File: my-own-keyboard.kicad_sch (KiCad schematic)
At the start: 138 parts, among them J1 CX70M-24P1, SW1 Reset SW, SW10 Key_SW, SW11 Key_SW, SW12 Key_SW, SW13 Key_SW, SW14 Key_SW, SW15 Key_SW, SW16 Key_SW, SW17 Key_SW, SW18 Key_SW, SW19 Key_SW, SW2 Key_SW, SW20 Key_SW, SW21 Key_SW, SW22 Key_SW, SW23 Key_SW, SW24 Key_SW, SW25 Key_SW, SW26 Key_SW, SW27 Key_SW, SW28 Key_SW, SW29 Key_SW, SW3 Key_SW, SW30 Key_SW, SW31 Key_SW, SW32 Key_SW, SW33 Key_SW, SW34 Key_SW, SW35 Key_SW, SW36 Key_SW, SW37 Key_SW, SW38 Key_SW, SW39 Key_SW, SW4 Key_SW, SW40 Key_SW, SW41 Key_SW, SW42 Key_SW, SW43 Key_SW, SW44 Key_SW, SW45 Key_SW, SW46 Key_SW, SW47 Key_SW, SW48 Key_SW, SW49 Key_SW, SW5 Key_SW, SW50 Key_SW, SW51 Key_SW, SW52 Key_SW, SW53 Key_SW, SW54 Key_SW, SW55 Key_SW, SW56 Key_SW, SW57 Key_SW, SW58 Key_SW, SW59 Key_SW, SW6 Key_SW, SW60 Key_SW, SW61 Key_SW, SW62 Key_SW, SW7 Key_SW, SW8 Key_SW, SW9 Key_SW, U1 ATmega32U4-A, Y1 16MHz

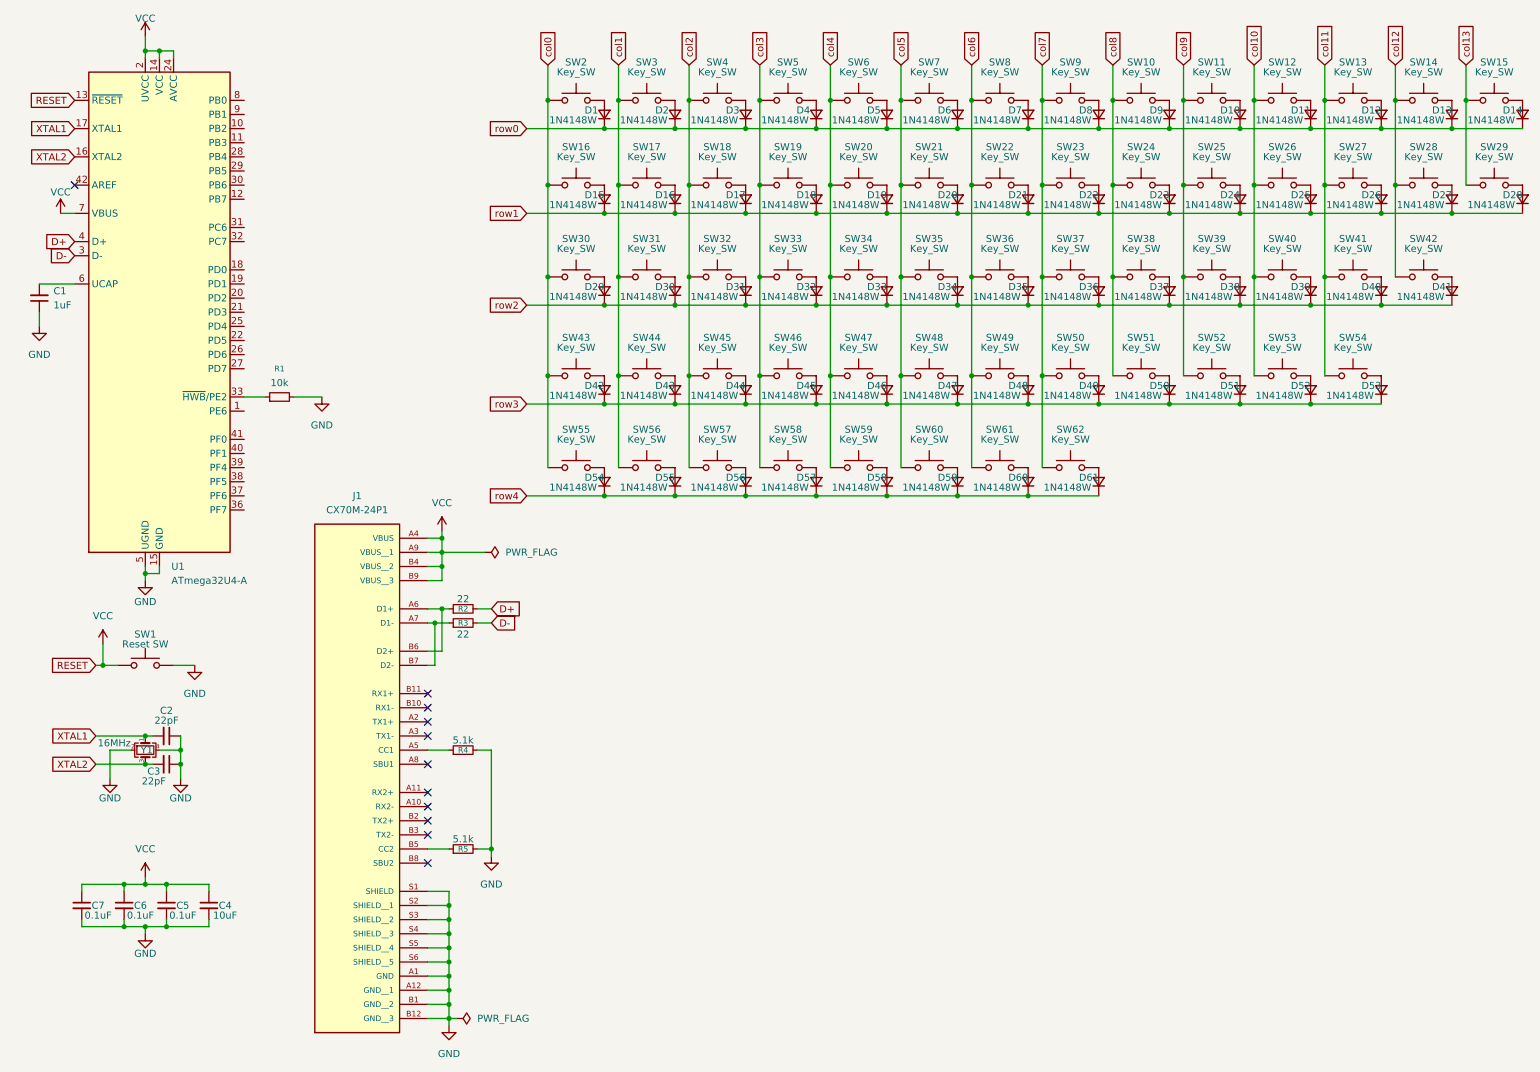
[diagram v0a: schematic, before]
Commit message: completed creating the first circuit
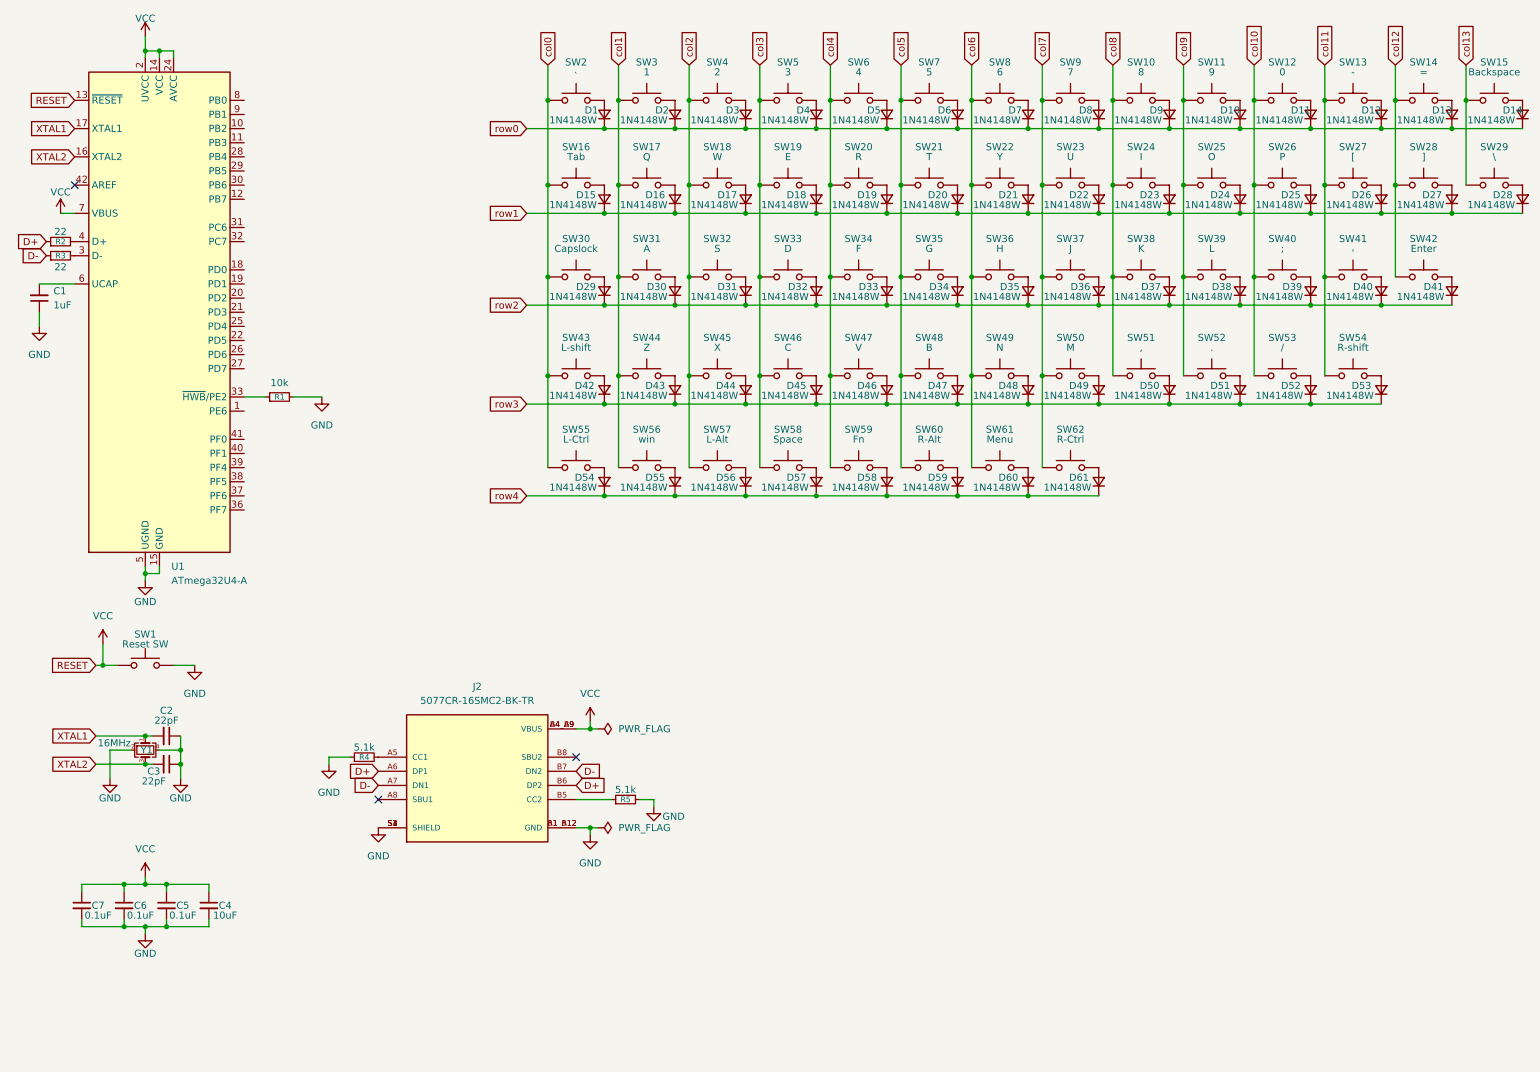
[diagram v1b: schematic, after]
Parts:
- removed J1: CX70M-24P1, CX70M-24P1:HRS_CX70M-24P1, symbol CX70M-24P1:CX70M-24P1
- added J2: 5077CR-16SMC2-BK-TR, 5077CR-16SMC2-BK-TR:NELTRON_5077CR-16SMC2-BK-TR, symbol 5077CR-16SMC2-BK-TR:5077CR-16SMC2-BK-TR
- C1, C2, C3, C4, C5, C6, C7: footprint (none) -> Capacitor_SMD:C_0603_1608Metric
- D1, D10, D11, D12, D13, D14, D15, D16, D17, D18, D19, D2, D20, D21, D22, D23, D24, D25, D26, D27, D28, D29, D3, D30, D31, D32, D33, D34, D35, D36, D37, D38, D39, D4, D40, D41, D42, D43, D44, D45, D46, D47, D48, D49, D5, D50, D51, D52, D53, D54, D55, D56, D57, D58, D59, D6, D60, D61, D7, D8, D9: footprint (none) -> kbd:D3_TH_SMD
- R1, R2, R3, R4, R5: footprint (none) -> Resistor_SMD:R_0603_1608Metric
- SW1: footprint (none) -> kbd:ResetSW
- SW10: value Key_SW -> 8; footprint (none) -> BrownSugar_KBD:CherryMX_Hotswap_via_1U
- SW11: value Key_SW -> 9; footprint (none) -> BrownSugar_KBD:CherryMX_Hotswap_via_1U
- SW12: value Key_SW -> 0; footprint (none) -> BrownSugar_KBD:CherryMX_Hotswap_via_1U
- SW13: value Key_SW -> -; footprint (none) -> BrownSugar_KBD:CherryMX_Hotswap_via_1U
- SW14: value Key_SW -> =; footprint (none) -> BrownSugar_KBD:CherryMX_Hotswap_via_1U
- SW15: value Key_SW -> Backspace; footprint (none) -> BrownSugar_KBD:CherryMX_Hotswap_via_2U
- SW16: value Key_SW -> Tab; footprint (none) -> BrownSugar_KBD:CherryMX_Hotswap_via_1.5U
- SW17: value Key_SW -> Q; footprint (none) -> BrownSugar_KBD:CherryMX_Hotswap_via_1U
- SW18: value Key_SW -> W; footprint (none) -> BrownSugar_KBD:CherryMX_Hotswap_via_1U
- SW19: value Key_SW -> E; footprint (none) -> BrownSugar_KBD:CherryMX_Hotswap_via_1U
- SW2: value Key_SW -> `; footprint (none) -> BrownSugar_KBD:CherryMX_Hotswap_via_1U
- SW20: value Key_SW -> R; footprint (none) -> BrownSugar_KBD:CherryMX_Hotswap_via_1U
- SW21: value Key_SW -> T; footprint (none) -> BrownSugar_KBD:CherryMX_Hotswap_via_1U
- SW22: value Key_SW -> Y; footprint (none) -> BrownSugar_KBD:CherryMX_Hotswap_via_1U
- SW23: value Key_SW -> U; footprint (none) -> BrownSugar_KBD:CherryMX_Hotswap_via_1U
- SW24: value Key_SW -> I; footprint (none) -> BrownSugar_KBD:CherryMX_Hotswap_via_1U
- SW25: value Key_SW -> O; footprint (none) -> BrownSugar_KBD:CherryMX_Hotswap_via_1U
- SW26: value Key_SW -> P; footprint (none) -> BrownSugar_KBD:CherryMX_Hotswap_via_1U
- SW27: value Key_SW -> [; footprint (none) -> BrownSugar_KBD:CherryMX_Hotswap_via_1U
- SW28: value Key_SW -> ]; footprint (none) -> BrownSugar_KBD:CherryMX_Hotswap_via_1U
- SW29: value Key_SW -> \; footprint (none) -> BrownSugar_KBD:CherryMX_Hotswap_via_1.5U
- SW3: value Key_SW -> 1; footprint (none) -> BrownSugar_KBD:CherryMX_Hotswap_via_1U
- SW30: value Key_SW -> Capslock; footprint (none) -> BrownSugar_KBD:CherryMX_Hotswap_via_1.75U
- SW31: value Key_SW -> A; footprint (none) -> BrownSugar_KBD:CherryMX_Hotswap_via_1U
- SW32: value Key_SW -> S; footprint (none) -> BrownSugar_KBD:CherryMX_Hotswap_via_1U
- SW33: value Key_SW -> D; footprint (none) -> BrownSugar_KBD:CherryMX_Hotswap_via_1U
- SW34: value Key_SW -> F; footprint (none) -> BrownSugar_KBD:CherryMX_Hotswap_via_1U
- SW35: value Key_SW -> G; footprint (none) -> BrownSugar_KBD:CherryMX_Hotswap_via_1U
- SW36: value Key_SW -> H; footprint (none) -> BrownSugar_KBD:CherryMX_Hotswap_via_1U
- SW37: value Key_SW -> J; footprint (none) -> BrownSugar_KBD:CherryMX_Hotswap_via_1U
- SW38: value Key_SW -> K; footprint (none) -> BrownSugar_KBD:CherryMX_Hotswap_via_1U
- SW39: value Key_SW -> L; footprint (none) -> BrownSugar_KBD:CherryMX_Hotswap_via_1U
- SW4: value Key_SW -> 2; footprint (none) -> BrownSugar_KBD:CherryMX_Hotswap_via_1U
- SW40: value Key_SW -> ;; footprint (none) -> BrownSugar_KBD:CherryMX_Hotswap_via_1U
- SW41: value Key_SW -> '; footprint (none) -> BrownSugar_KBD:CherryMX_Hotswap_via_1U
- SW42: value Key_SW -> Enter; footprint (none) -> BrownSugar_KBD:CherryMX_Hotswap_via_2.25U
- SW43: value Key_SW -> L-shift; footprint (none) -> BrownSugar_KBD:CherryMX_Hotswap_via_2.25U
- SW44: value Key_SW -> Z; footprint (none) -> BrownSugar_KBD:CherryMX_Hotswap_via_1U
- SW45: value Key_SW -> X; footprint (none) -> BrownSugar_KBD:CherryMX_Hotswap_via_1U
- SW46: value Key_SW -> C; footprint (none) -> BrownSugar_KBD:CherryMX_Hotswap_via_1U
- SW47: value Key_SW -> V; footprint (none) -> BrownSugar_KBD:CherryMX_Hotswap_via_1U
- SW48: value Key_SW -> B; footprint (none) -> BrownSugar_KBD:CherryMX_Hotswap_via_1U
- SW49: value Key_SW -> N; footprint (none) -> BrownSugar_KBD:CherryMX_Hotswap_via_1U
- SW5: value Key_SW -> 3; footprint (none) -> BrownSugar_KBD:CherryMX_Hotswap_via_1U
- SW50: value Key_SW -> M; footprint (none) -> BrownSugar_KBD:CherryMX_Hotswap_via_1U
- SW51: value Key_SW -> ,; footprint (none) -> BrownSugar_KBD:CherryMX_Hotswap_via_1U
- SW52: value Key_SW -> .; footprint (none) -> BrownSugar_KBD:CherryMX_Hotswap_via_1U
- SW53: value Key_SW -> /; footprint (none) -> BrownSugar_KBD:CherryMX_Hotswap_via_1U
- SW54: value Key_SW -> R-shift; footprint (none) -> BrownSugar_KBD:CherryMX_Hotswap_via_2.75U
- SW55: value Key_SW -> L-Ctrl; footprint (none) -> BrownSugar_KBD:CherryMX_Hotswap_via_1.25U
- SW56: value Key_SW -> win; footprint (none) -> BrownSugar_KBD:CherryMX_Hotswap_via_1.25U
- SW57: value Key_SW -> L-Alt; footprint (none) -> BrownSugar_KBD:CherryMX_Hotswap_via_1.25U
- SW58: value Key_SW -> Space; footprint (none) -> BrownSugar_KBD:CherryMX_Hotswap_via_3U
- SW59: value Key_SW -> Fn; footprint (none) -> BrownSugar_KBD:CherryMX_Hotswap_via_3U
- SW6: value Key_SW -> 4; footprint (none) -> BrownSugar_KBD:CherryMX_Hotswap_via_1U
- SW60: value Key_SW -> R-Alt; footprint (none) -> BrownSugar_KBD:CherryMX_Hotswap_via_1.25U
- SW61: value Key_SW -> Menu; footprint (none) -> BrownSugar_KBD:CherryMX_Hotswap_via_1.25U
- SW62: value Key_SW -> R-Ctrl; footprint (none) -> BrownSugar_KBD:CherryMX_Hotswap_via_1.25U
- SW7: value Key_SW -> 5; footprint (none) -> BrownSugar_KBD:CherryMX_Hotswap_via_1U
- SW8: value Key_SW -> 6; footprint (none) -> BrownSugar_KBD:CherryMX_Hotswap_via_1U
- SW9: value Key_SW -> 7; footprint (none) -> BrownSugar_KBD:CherryMX_Hotswap_via_1U
- Y1: footprint (none) -> Crystal:Crystal_SMD_3225-4Pin_3.2x2.5mm
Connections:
- net D+: now also R2.1, J2.A6 (DP1), J2.B6 (DP2); no longer R2.2, U1.4 (D+)
- net D-: now also R3.1, J2.A7 (DN1), J2.B7 (DN2); no longer R3.2, U1.3 (D-)
- net GND: now also R4.1, J2.A1_B12 (GND), J2.B1_A12 (GND), J2.S1 (SHIELD), J2.S2 (SHIELD), J2.S3 (SHIELD), J2.S4 (SHIELD); no longer R4.2
- net VCC: now also J2.A4_B9 (VBUS), J2.B4_A9 (VBUS)
- net at R5.1: now also J2.B5 (CC2)
- new net: J2.A5 (CC1), R4.2
- new net: R3.2, U1.3 (D-)
- new net: R2.2, U1.4 (D+)
- no-connect marks 11 -> 3

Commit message: added a rotary encoder
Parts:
- added D62: 1N4148W, kbd:D3_TH_SMD, symbol Device:D_Small
- added SW63: RotaryEncoder_Switch, Rotary_Encoder:RotaryEncoder_Alps_EC12E-Switch_Vertical_H20mm, symbol Device:RotaryEncoder_Switch
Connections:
- net GND: now also SW63.C
- net col8: now also SW63.S2
- net row4: now also D62.1 (K)
- new net: D62.2 (A), SW63.S1
- new net RE_A: SW63.A
- new net RE_B: SW63.B
- no-connect marks 3 -> 8

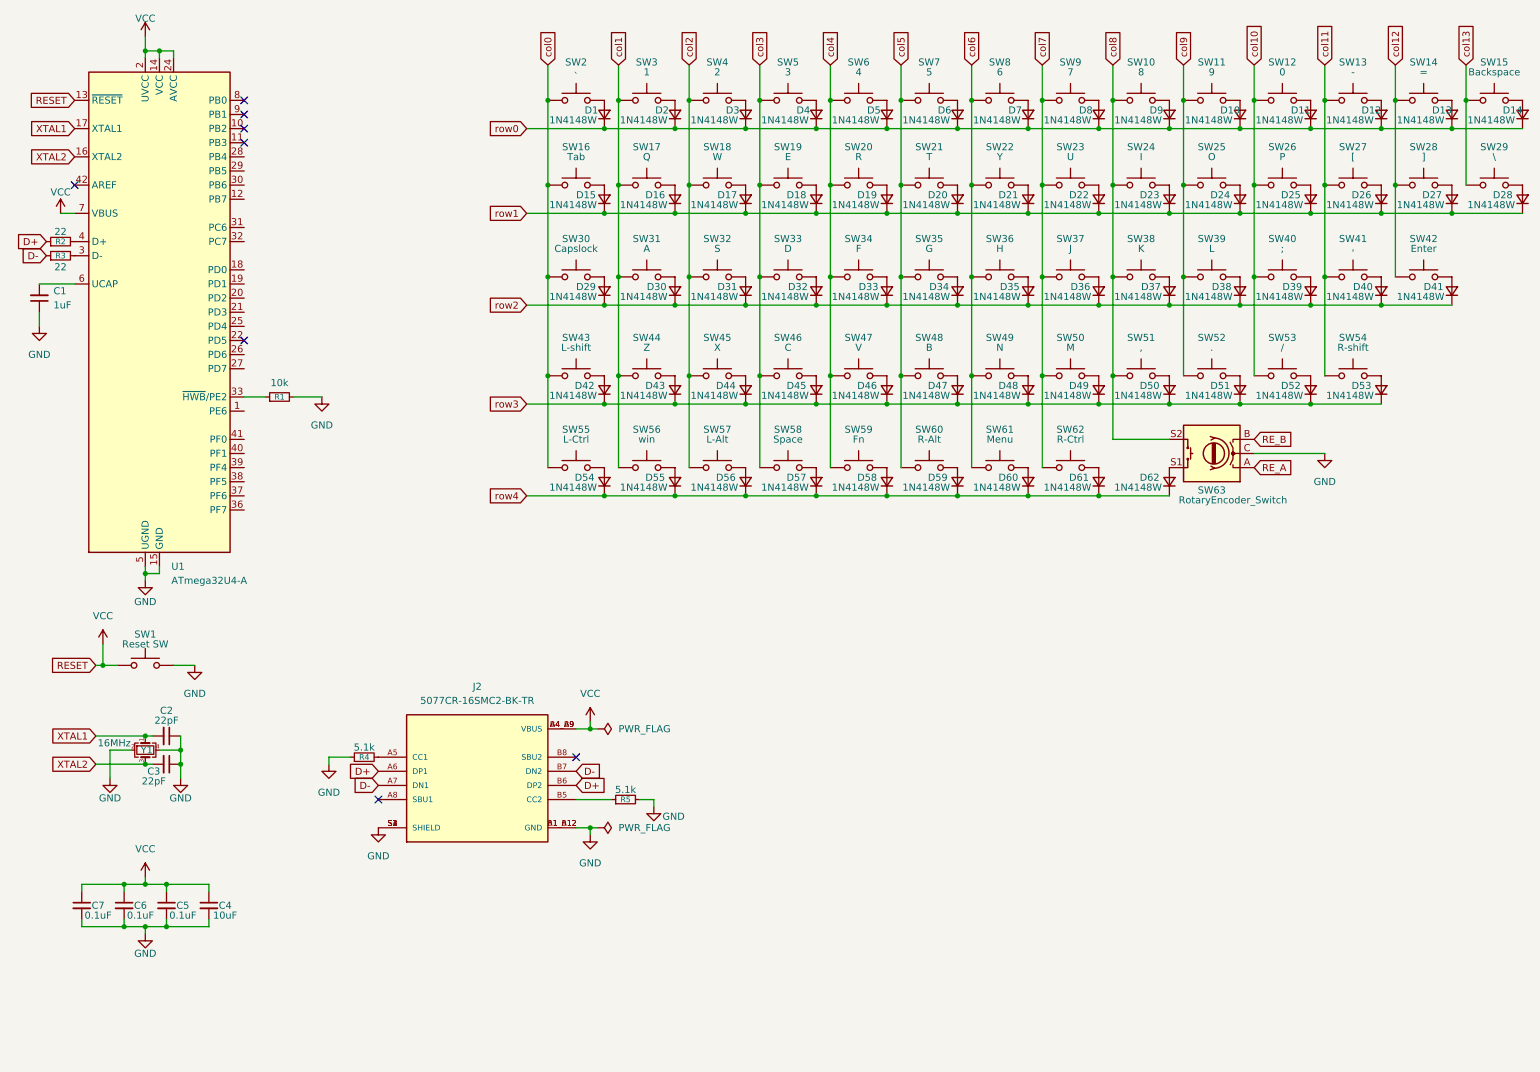
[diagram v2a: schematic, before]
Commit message: put the footprints and defined the design rules
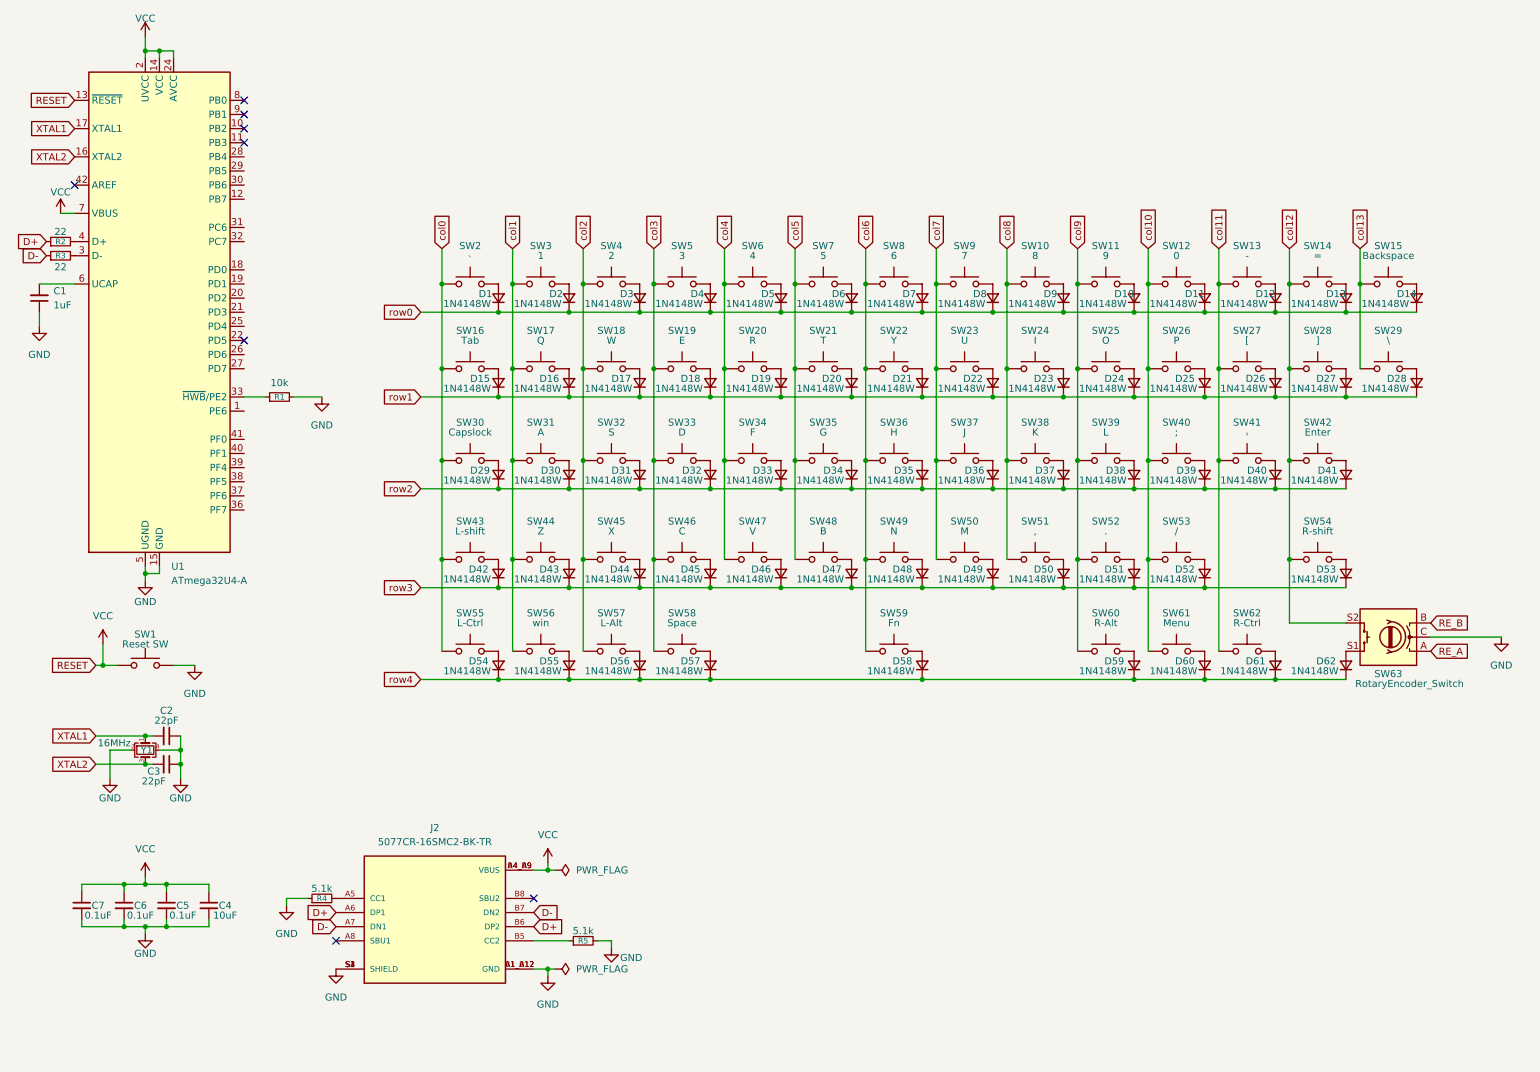
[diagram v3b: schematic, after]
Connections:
- net col10: now also SW61.1
- net col11: now also SW62.1; no longer SW54.1
- net col12: now also SW54.1, SW63.S2
- net col4: no longer SW59.1
- net col5: no longer SW60.1
- net col6: now also SW59.1; no longer SW61.1
- net col7: no longer SW62.1
- net col8: no longer SW63.S2
- net col9: now also SW60.1
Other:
- moved on the sheet: D1, D10, D11, D12, D13, D14, D15, D16, D17, D18, D19, D2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

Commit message: wired
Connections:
- net GND: now also SW1.1; no longer SW1.2
- net VCC: now also SW1.2; no longer SW1.1
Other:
- moved on the sheet: C1, R1, R2, R3, SW1, U1

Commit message: completed wiring
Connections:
- net RE_A: now also U1.18 (PD0)
- net RE_B: now also U1.19 (PD1)
- net col0: now also U1.20 (PD2)
- net col1: now also U1.21 (PD3)
- net col10: now also U1.30 (PB6)
- net col11: now also U1.38 (PF5)
- net col12: now also U1.39 (PF4)
- net col13: now also U1.8 (PB0)
- net col2: now also U1.22 (PD5)
- net col3: now also U1.25 (PD4)
- net col4: now also U1.26 (PD6)
- net col5: now also U1.27 (PD7)
- net col6: now also U1.28 (PB4)
- net col7: now also U1.29 (PB5)
- net col8: now also U1.32 (PC7)
- net col9: now also U1.31 (PC6)
- net row0: now also U1.1 (PE6)
- net row1: now also U1.41 (PF0)
- net row2: now also U1.40 (PF1)
- net row3: now also U1.37 (PF6)
- net row4: now also U1.36 (PF7)
- net MOSI: now reaches U1.10 (PB2)
- net MISO: now reaches U1.11 (PB3)
- net SCK: now reaches U1.9 (PB1)
- no-connect marks 8 -> 4
